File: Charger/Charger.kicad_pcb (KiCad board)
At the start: 2 copper layers, 106 parts, among them J1 Bat_ballanser_conn, J2 Battery_conn, Q1 BC846BW, Q10 MJD45H11T4, Q11 MJD45H11T4, Q12 MJD45H11T4, Q13 BC846BW, Q14 MJD31CT4, Q15 BUJ302AD, Q16 BUJ302AD, Q17 IRF7404, Q18 IRF7404, Q19 BC846BW, Q2 BC846BW, Q3 BC846BW, Q4 MJD45H11T4, Q5 MJD45H11T4, Q6 MJD45H11T4, Q7 BC846BW, Q8 BC846BW, Q9 BC846BW, U1 LM2904, U10 MCP6001-OT, U11 MCP6001-OT, U12 ACS712xLCTR-20A, U2 LM2904, U3 LM2904, U4 LM2904, U5 LM2904, U6 LM2904, U7 MCP6001-OT, U8 MCP6001-OT, U9 MCP6001-OT

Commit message: rozpoczęcie PCB
zrobiony balanser
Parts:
- added C16: 1uF, Capacitor_SMD:C_0805_2012Metric_Pad1.18x1.45mm_HandSolder, F.Cu at (-99.2, 61.8)
- added C17: 1uF, Capacitor_SMD:C_0805_2012Metric_Pad1.18x1.45mm_HandSolder, F.Cu at (-99.2, 64.8)
- added C18: 1uF, Capacitor_SMD:C_0805_2012Metric_Pad1.18x1.45mm_HandSolder, F.Cu at (-99.2, 67.8)
- added C19: 1uF, Capacitor_SMD:C_0805_2012Metric_Pad1.18x1.45mm_HandSolder, F.Cu at (-99.2, 70.8)
- added C20: 1uF, Capacitor_SMD:C_0805_2012Metric_Pad1.18x1.45mm_HandSolder, F.Cu at (-99.2, 73.8)
- added C21: 1uF, Capacitor_SMD:C_0805_2012Metric_Pad1.18x1.45mm_HandSolder, F.Cu at (-99.2, 76.8)
- added C22: 470u, Library:CP_Elec_12.5x13.5, F.Cu at (-114.6, 72.0)
- added C23: 470u, Library:CP_Elec_12.5x13.5, F.Cu at (-114.6, 86.6)
- added C24: 470u, Library:CP_Elec_12.5x13.5, F.Cu at (-20.3, 42.8)
- added C25: 470u, Library:CP_Elec_12.5x13.5, F.Cu at (-20.3, 57.4)
- added C26: 22u, Capacitor_SMD:CP_Elec_4x5.4, F.Cu at (-15.4, 67.7)
- added C27: 100n, Capacitor_SMD:C_0805_2012Metric_Pad1.18x1.45mm_HandSolder, F.Cu at (-10.0, 37.1)
- added C28: 100n, Capacitor_SMD:C_0805_2012Metric_Pad1.18x1.45mm_HandSolder, F.Cu at (-10.0, 40.1)
- added C29: 100n, Capacitor_SMD:C_0805_2012Metric_Pad1.18x1.45mm_HandSolder, F.Cu at (-10.0, 43.1)
- added C30: 22u, Capacitor_SMD:CP_Elec_4x5.4, F.Cu at (-15.4, 73.5)
- added C31: 100n, Capacitor_SMD:C_0805_2012Metric_Pad1.18x1.45mm_HandSolder, F.Cu at (-10.0, 46.1)
- added C7: 470u, Library:CP_Elec_12.5x13.5, F.Cu at (-114.6, 42.8)
- added C8: 470u, Library:CP_Elec_12.5x13.5, F.Cu at (-114.6, 57.4)
- added D1: LL103A, Diode_SMD:D_MiniMELF, F.Cu at (-82.8, 73.7)
- added D2: LL103A, Diode_SMD:D_MiniMELF, F.Cu at (-82.8, 77.1)
- added D3: LL103A, Diode_SMD:D_MiniMELF, F.Cu at (-82.8, 80.4)
- added D4: B540C, Diode_SMD:D_3220_8050Metric_Pad2.65x5.15mm_HandSolder, F.Cu at (-91.4, 75.5)
- added D5: B540C, Diode_SMD:D_3220_8050Metric_Pad2.65x5.15mm_HandSolder, F.Cu at (-91.4, 82.3)
- added D6: SS26, Diode_SMD:D_SMA, F.Cu at (-25.1, 75.3)
- added J3: Power_conn, Connector_AMASS:AMASS_XT60PW-F_1x02_P7.20mm_Horizontal, F.Cu at (-16.9, 115.9)
- added L1: 47uH, Inductor_SMD:L_Bourns_SRP1038C_10.0x10.0mm, F.Cu at (-82.0, 41.5)
- added L2: 47uH, Inductor_SMD:L_Bourns_SRP1038C_10.0x10.0mm, F.Cu at (-82.0, 53.3)
- added L3: 330u, Inductor_SMD:L_Bourns_SRR1208_12.7x12.7mm, F.Cu at (-39.1, 67.4)
- added R61: 10k, Resistor_SMD:R_0805_2012Metric_Pad1.20x1.40mm_HandSolder, F.Cu at (-94.4, 64.7)
- added R62: 5.1k, Resistor_SMD:R_0805_2012Metric_Pad1.20x1.40mm_HandSolder, F.Cu at (-94.4, 67.7)
- added R63: 1.2k, Resistor_SMD:R_0805_2012Metric_Pad1.20x1.40mm_HandSolder, F.Cu at (-94.4, 70.6)
- added R64: 10K, Resistor_SMD:R_0805_2012Metric_Pad1.20x1.40mm_HandSolder, F.Cu at (-89.7, 61.8)
- added R65: 10K, Resistor_SMD:R_0805_2012Metric_Pad1.20x1.40mm_HandSolder, F.Cu at (-89.7, 64.7)
- added R66: 10k, Resistor_SMD:R_0805_2012Metric_Pad1.20x1.40mm_HandSolder, F.Cu at (-89.7, 67.7)
- added R67: 1.2k, Resistor_SMD:R_0805_2012Metric_Pad1.20x1.40mm_HandSolder, F.Cu at (-89.7, 70.6)
- added R68: 10k, Resistor_SMD:R_0805_2012Metric_Pad1.20x1.40mm_HandSolder, F.Cu at (-84.9, 61.8)
- added R69: 1.2k, Resistor_SMD:R_0805_2012Metric_Pad1.20x1.40mm_HandSolder, F.Cu at (-84.9, 64.7)
- added R70: 2k, Resistor_SMD:R_0805_2012Metric_Pad1.20x1.40mm_HandSolder, F.Cu at (-84.9, 67.7)
- added R71: 1.2k, Resistor_SMD:R_0805_2012Metric_Pad1.20x1.40mm_HandSolder, F.Cu at (-84.9, 70.6)
- added U13: MCP6001-OT, Package_TO_SOT_SMD:SOT-23-5, F.Cu at (-104.2, 62.7)
- added U14: MCP6001-OT, Package_TO_SOT_SMD:SOT-23-5, F.Cu at (-104.2, 67.3)
- added U15: MCP6001-OT, Package_TO_SOT_SMD:SOT-23-5, F.Cu at (-104.2, 71.9)
- added U16: MCP6001-OT, Package_TO_SOT_SMD:SOT-23-5, F.Cu at (-104.2, 76.5)
- added U17: XL4015, Package_TO_SOT_SMD:TO-263-5_TabPin3, F.Cu at (-96.0, 41.8)
- added U18: XL4015, Package_TO_SOT_SMD:TO-263-5_TabPin3, F.Cu at (-96.0, 54.1)
- added U19: MCP6001-OT, Package_TO_SOT_SMD:SOT-23-5, F.Cu at (-104.2, 81.2)
- added U20: LM2575-12BU, Package_TO_SOT_SMD:TO-263-5_TabPin3, F.Cu at (-36.1, 41.8)
- added U21: L7805, Package_TO_SOT_SMD:TO-263-2, F.Cu at (-36.1, 54.1)
- added U22: LDI1117-3.3, Package_TO_SOT_SMD:SOT-223-3_TabPin2, F.Cu at (-24.2, 69.0)
- added U23: RaspberryPi_Pico, Module_RaspberryPi_Pico:RaspberryPi_Pico_Common, F.Cu at (-60.9, 83.7)
- R13, R14, R15, R16, R17, R18, R19, R20, R21, R28, R29, R30, R34, R35, R36, R37, R38, R39, R40, R41, R42, R7, R8, R9: moved to B.Cu
- R44: value 5.1k -> 2k
- moved U12 297.4 mm to (-68.8, 129.3), turned to 0 degrees
- moved Q17 288.9 mm to (-68.8, 116.2)
- moved R55 286.4 mm to (-62.2, 120.2), turned to 0 degrees
- moved C9 285.4 mm to (-57.4, 114.3)
- moved R46 284.1 mm to (-62.2, 117.2), turned to 0 degrees
- moved Q18 282.6 mm to (-68.8, 122.7), turned to 0 degrees
- moved C10 282.5 mm to (-57.4, 117.3)
- moved R56 282.5 mm to (-62.2, 123.1), turned to 0 degrees
- moved R45 282.3 mm to (-62.2, 114.3), turned to 0 degrees
- moved U10 281.3 mm to (-62.0, 127.0), turned to 0 degrees
- moved Q19 276.3 mm to (-57.2, 126.6), turned to 0 degrees
- moved C11 275.8 mm to (-57.4, 120.3)
- moved J2 270.1 mm to (-41.7, 97.0), turned to 0 degrees
- moved R44 189.1 mm to (-94.4, 61.8)
- moved R50 143.5 mm to (-27.2, 131.3)
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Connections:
- net /Pomiar pradu/P+ renamed /Ladowarka/Vout
- net /Pomiar pradu/hall_sensor renamed /Ladowarka/Hall
- R44 pad 1: Net-(R44-Pad1) -> GND
- R44 pad 2: Net-(U7-+) -> Net-(R44-Pad2)
- R47 pad 2: Net-(R44-Pad1) -> Net-(U7-+)
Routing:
- net GND: track 46.3 -> 0.00 mm
- net /Balanser/Vballans: track 62.8 -> 106.5 mm
- net +12V: track 57.9 -> 14.5 mm
- net /Balanser/B5: track 62.5 -> 26.6 mm, vias 36 -> 41
- net /Balanser/B4: track 53.3 -> 22.8 mm, vias 36 -> 41
- net /Balanser/B6: track 54.7 -> 30.1 mm
- net /Balanser/B3: track 45.9 -> 22.3 mm, vias 36 -> 41
- net /Balanser/B2: track 44.4 -> 26.2 mm, vias 36 -> 41
- net /Balanser/B1: track 51.7 -> 36.3 mm, vias 72 -> 41
- net Net-(U1A--): track 9.68 -> 21.9 mm, vias 0 -> 2
- net Net-(U5A--): track 8.18 -> 19.1 mm, vias 0 -> 2
- net Net-(U4A--): track 8.26 -> 19.1 mm, vias 0 -> 2
- net Net-(U2A--): track 8.92 -> 19.7 mm, vias 0 -> 2
- net Net-(U3A--): track 8.31 -> 18.9 mm, vias 0 -> 2
- net Net-(R13-Pad1): track 0.00 -> 3.97 mm, vias 0 -> 1
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- added copper zone on B.Cu, net (none)
- added copper zone on F.Cu, net (none)

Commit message: pcb up
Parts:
- removed C14: 100n, Capacitor_SMD:C_0805_2012Metric_Pad1.18x1.45mm_HandSolder
- removed U11, U14, U15, U16, U7, U8, U9: MCP6001-OT, Package_TO_SOT_SMD:SOT-23-5
- added C32: 1u, Capacitor_SMD:C_0805_2012Metric_Pad1.18x1.45mm_HandSolder, F.Cu at (119.3, 86.2)
- added C33: 1u, Capacitor_SMD:C_0805_2012Metric_Pad1.18x1.45mm_HandSolder, F.Cu at (101.0, 86.4)
- added C34: 1u, Capacitor_SMD:C_0805_2012Metric_Pad1.18x1.45mm_HandSolder, F.Cu at (114.9, 86.2)
- added C35: 1u, Capacitor_SMD:C_0805_2012Metric_Pad1.18x1.45mm_HandSolder, F.Cu at (129.5, 86.4)
- added C36: 100n, Capacitor_SMD:C_0805_2012Metric_Pad1.18x1.45mm_HandSolder, F.Cu at (99.1, 56.4)
- added C37: 100n, Capacitor_SMD:C_0805_2012Metric_Pad1.18x1.45mm_HandSolder, F.Cu at (155.8, 62.3)
- added C38: 100n, Capacitor_SMD:C_0805_2012Metric_Pad1.18x1.45mm_HandSolder, F.Cu at (103.1, 125.5)
- added D7: SS26, Diode_SMD:D_SMA, F.Cu at (119.0, 126.4)
- added F1: Fuse_Small, Fuse:Fuse_2010_5025Metric_Pad1.52x2.65mm_HandSolder, F.Cu at (125.8, 126.4)
- added F2: Fuse_Small, Fuse:Fuse_2010_5025Metric_Pad1.52x2.65mm_HandSolder, F.Cu at (211.8, 109.5)
- added J4: Screen_SPInCtrlnPwr_Conn, Connector_PinHeader_2.54mm:PinHeader_1x10_P2.54mm_Vertical, F.Cu at (144.3, 54.6)
- added J5: User_Interface_Conn, Connector_PinHeader_2.54mm:PinHeader_1x07_P2.54mm_Horizontal, F.Cu at (149.4, 83.5)
- added J6: 1/0_Select_Conn, Connector_PinHeader_2.54mm:PinHeader_1x03_P2.54mm_Vertical, F.Cu at (124.0, 50.2)
- added J8: Temp_Sens_Conn, Connector_PinHeader_2.54mm:PinHeader_1x03_P2.54mm_Vertical, F.Cu at (105.6, 85.6)
- added R72: 10k, Resistor_SMD:R_0805_2012Metric_Pad1.20x1.40mm_HandSolder, F.Cu at (95.9, 83.0)
- added R73: 1.2k, Resistor_SMD:R_0805_2012Metric_Pad1.20x1.40mm_HandSolder, F.Cu at (119.3, 82.8)
- added R75: 1.2k, Resistor_SMD:R_0805_2012Metric_Pad1.20x1.40mm_HandSolder, F.Cu at (100.9, 83.0)
- added R76: 1.2k, Resistor_SMD:R_0805_2012Metric_Pad1.20x1.40mm_HandSolder, F.Cu at (114.9, 82.8)
- added R77: 1.2k, Resistor_SMD:R_0805_2012Metric_Pad1.20x1.40mm_HandSolder, F.Cu at (124.3, 82.8)
- added R78: 10k, Resistor_SMD:R_0805_2012Metric_Pad1.20x1.40mm_HandSolder, F.Cu at (124.4, 86.2)
- added R79: 10k, Resistor_SMD:R_0805_2012Metric_Pad1.20x1.40mm_HandSolder, F.Cu at (129.4, 82.8)
- added U24: CD4051B, Package_SO:SO-16_5.3x10.2mm_P1.27mm, F.Cu at (153.0, 69.4)
- added U25: MCP6004, Package_SO:SOIC-14_3.9x8.7mm_P1.27mm, F.Cu at (62.0, 160.6)
- U13: value MCP6001-OT -> MCP6004; footprint Package_TO_SOT_SMD:SOT-23-5 -> Package_SO:SOIC-14_3.9x8.7mm_P1.27mm
- U23: footprint Module_RaspberryPi_Pico:RaspberryPi_Pico_Common -> Module_RaspberryPi_Pico:RaspberryPi_Pico_Common_SMD
- moved C8 322.5 mm to (192.9, 154.7), turned to 90 degrees
- moved C22 302.1 mm to (175.8, 155.4), turned to 90 degrees
- moved C20 296.1 mm to (190.2, 136.3), turned to -90 degrees
- moved C7 293.0 mm to (155.6, 156.2)
- moved C23 291.6 mm to (164.1, 172.4), turned to -90 degrees
- moved U17 282.8 mm to (170.2, 137.3), turned to -90 degrees
- moved D4 280.8 mm to (181.7, 140.9)
- moved L1 279.9 mm to (182.9, 131.8)
- moved Q16 275.1 mm to (233.7, 112.4), turned to 90 degrees
- moved C18 273.6 mm to (168.4, 124.6), turned to -90 degrees
- moved C17 271.9 mm to (166.1, 124.6), turned to 90 degrees
- moved U18 267.4 mm to (158.1, 137.3), turned to -90 degrees
- moved Q15 267.1 mm to (226.3, 112.4), turned to 90 degrees
- moved C19 261.2 mm to (156.3, 124.7), turned to -90 degrees
- moved C16 260.9 mm to (154.0, 124.7), turned to 90 degrees
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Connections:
- C12 pad 1: /Sztuczne_obciazenie/+5V -> +5V
- C13 pad 1: /Sztuczne_obciazenie/+5V -> +5V
- C15 pad 1: /Sztuczne_obciazenie/+5V -> +5V
- C16 pad 1: /Ladowarka/Vin -> +36V
- C17 pad 1: /Ladowarka/Vin -> +36V
- C18 pad 1: /Ladowarka/Vin -> +36V
- C19 pad 1: /Ladowarka/Vin -> +36V
- C23 pad 1: /Ladowarka/Vin -> +36V
- C25 pad 1: /Ladowarka/Vin -> +36V
- C7 pad 1: /Ladowarka/Vin -> +36V
- D1 pad 2: /Ladowarka/Off -> GPIO2
- J3 pad 2: /Ladowarka/Vin -> Net-(J3-Pin_2)
- Q14 pad 2: /Ladowarka/Vout -> /Sztuczne_obciazenie/B+
- Q15 pad 2: /Ladowarka/Vout -> /Sztuczne_obciazenie/B+
- Q16 pad 2: /Ladowarka/Vout -> /Sztuczne_obciazenie/B+
- Q19 pad 1: /Pomiar pradu/P_ON -> GPIO10
- R47 pad 1: /Sztuczne_obciazenie/set_I -> /MCU/LOAD_SetI
- R47 pad 2: Net-(U7-+) -> Net-(U13A-+)
- R48 pad 2: Net-(U7-+) -> Net-(U13A-+)
- R49 pad 1: /Sztuczne_obciazenie/EN -> GPIO8
- R49 pad 2: Net-(U8-+) -> Net-(U13C-+)
- R50 pad 2: Net-(U8-+) -> Net-(U13C-+)
- R51 pad 2: Net-(U9--) -> Net-(U13B--)
- R52 pad 1: Net-(U9--) -> Net-(U13B--)
- R52 pad 2: Net-(U11-+) -> Net-(U13D-+)
- R53 pad 1: Net-(U8--) -> Net-(U13C--)
- R53 pad 2: Net-(U9-+) -> Net-(U13B-+)
- R54 pad 1: Net-(U7--) -> Net-(U13A--)
- R54 pad 2: Net-(U9-+) -> Net-(U13B-+)
- R59 pad 2: /Ladowarka/Vout -> /Sztuczne_obciazenie/B+
- R61 pad 1: Net-(U13-+) -> Net-(U25A-+)
- R62 pad 2: Net-(U13-+) -> Net-(U25A-+)
- R64 pad 2: Net-(U13--) -> Net-(U25A--)
- U13 pad 1: Net-(U13--) -> Net-(U13A--)
- U13 pad 2: GND -> Net-(U13A--)
- U13 pad 3: Net-(U13-+) -> Net-(U13A-+)
- U13 pad 4: Net-(U13--) -> +5V
- U13 pad 5: +5V -> Net-(U13B-+)
- U17 pad 5: /Ladowarka/Vin -> +36V
- U18 pad 5: /Ladowarka/Vin -> +36V
- U20 pad 1: /Ladowarka/Vin -> +36V
- U23 pad 10: unconnected-(U23-GPIO7-Pad10) -> GPIO7
- U23 pad 11: unconnected-(U23-GPIO8-Pad11) -> GPIO8
- U23 pad 12: unconnected-(U23-GPIO9-Pad12) -> GPIO9
- U23 pad 14: unconnected-(U23-GPIO10-Pad14) -> GPIO10
- U23 pad 15: unconnected-(U23-GPIO11-Pad15) -> GPIO11
- U23 pad 16: unconnected-(U23-GPIO12-Pad16) -> GPIO12
- U23 pad 17: unconnected-(U23-GPIO13-Pad17) -> GPIO13
- U23 pad 19: unconnected-(U23-GPIO14-Pad19) -> GPIO14
- U23 pad 20: unconnected-(U23-GPIO15-Pad20) -> GPIO15
- U23 pad 21: unconnected-(U23-GPIO16-Pad21) -> GPIO16
- U23 pad 22: unconnected-(U23-GPIO17-Pad22) -> GPIO17
- U23 pad 24: unconnected-(U23-GPIO18-Pad24) -> GPIO18
- U23 pad 25: unconnected-(U23-GPIO19-Pad25) -> GPIO19
- U23 pad 26: unconnected-(U23-GPIO20-Pad26) -> GPIO20
- U23 pad 27: unconnected-(U23-GPIO21-Pad27) -> GPIO21
- U23 pad 29: unconnected-(U23-GPIO22-Pad29) -> GPIO22
- U23 pad 31: unconnected-(U23-GPIO26_ADC0-Pad31) -> ADC_0
- U23 pad 32: unconnected-(U23-GPIO27_ADC1-Pad32) -> GPIO27
- U23 pad 33: unconnected-(U23-AGND-Pad33) -> GND
- U23 pad 34: unconnected-(U23-GPIO28_ADC2-Pad34) -> GPIO28
- U23 pad 39: unconnected-(U23-VSYS-Pad39) -> +5V
- U23 pad 4: unconnected-(U23-GPIO2-Pad4) -> GPIO2
- U23 pad 5: unconnected-(U23-GPIO3-Pad5) -> GPIO3
- U23 pad 6: unconnected-(U23-GPIO4-Pad6) -> GPIO4
- U23 pad 9: unconnected-(U23-GPIO6-Pad9) -> GPIO6

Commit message: small update
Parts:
- F1: value Fuse_Small -> 10A
- moved C25 43.6 mm to (147.9, 173.8)
- moved C24 14.3 mm to (123.7, 165.5)
- moved J6 5.05 mm to (129.1, 50.2), turned to -90 degrees
- moved C22 1.78 mm to (177.4, 154.6)
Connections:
- J4 pad 2: GPIO19 -> GPIO16
- J4 pad 3: GPIO16 -> GPIO17
- J4 pad 4: GPIO17 -> GPIO18
- J4 pad 5: GPIO18 -> GPIO19
- J5 pad 2: GPIO14 -> GPIO15
- J5 pad 3: GPIO15 -> GPIO14

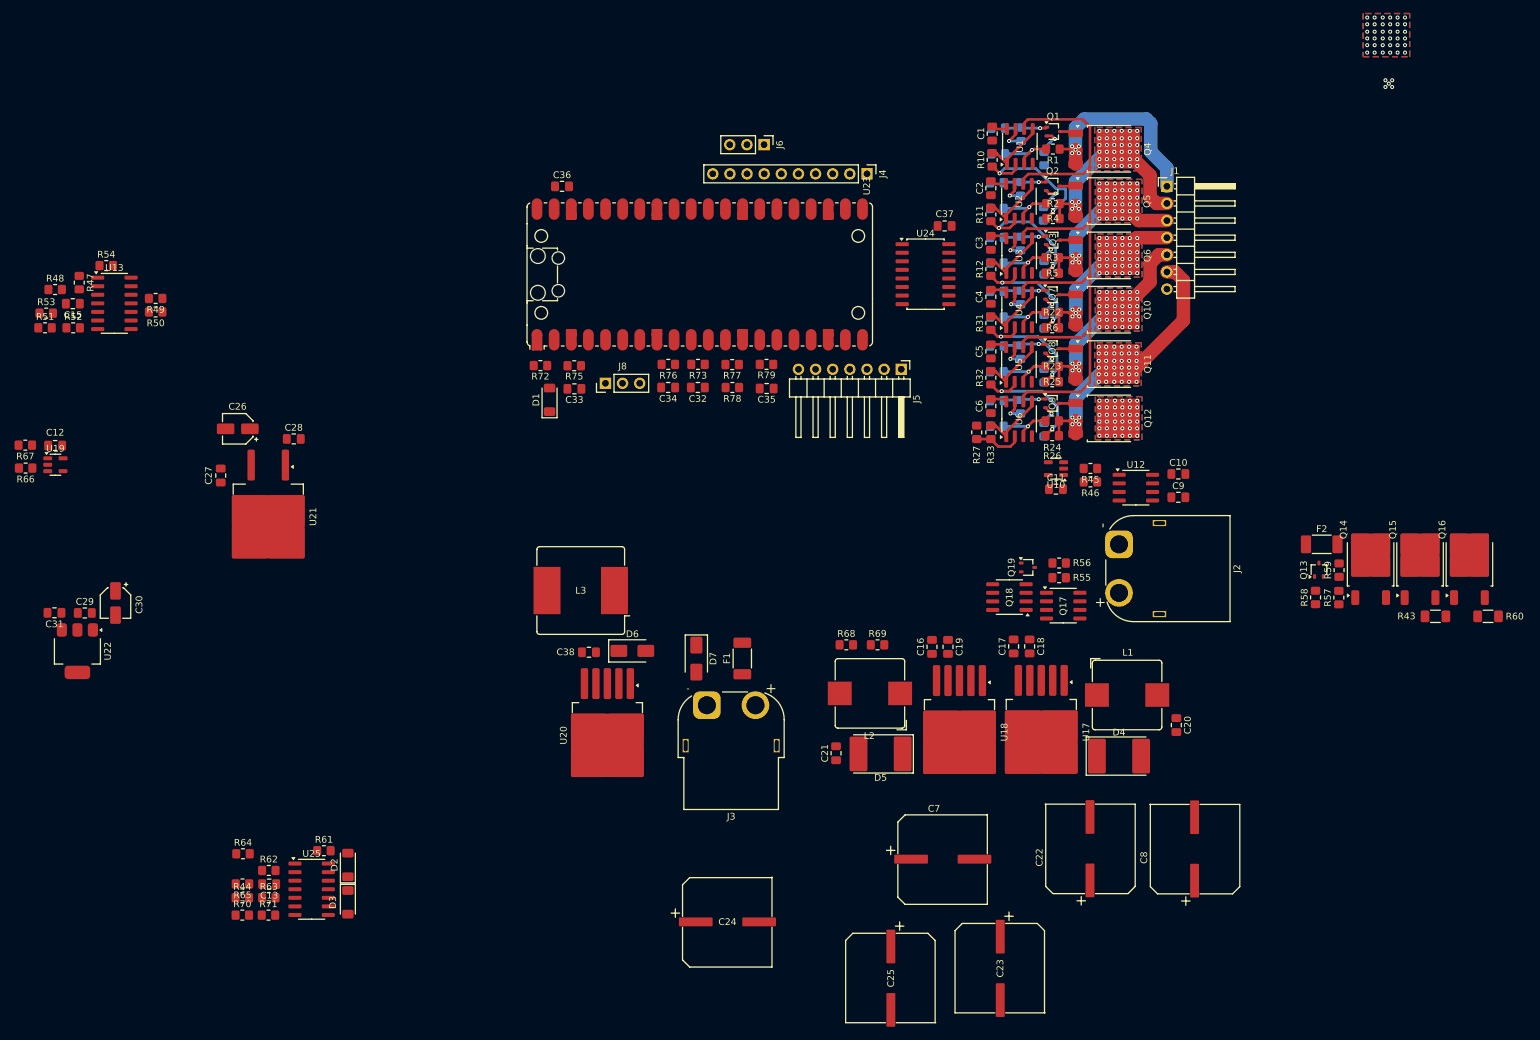
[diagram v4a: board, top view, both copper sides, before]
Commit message: pcb poukladane
usuniete 3 kondensatory
brak poligonow i odprowadzania ciepla
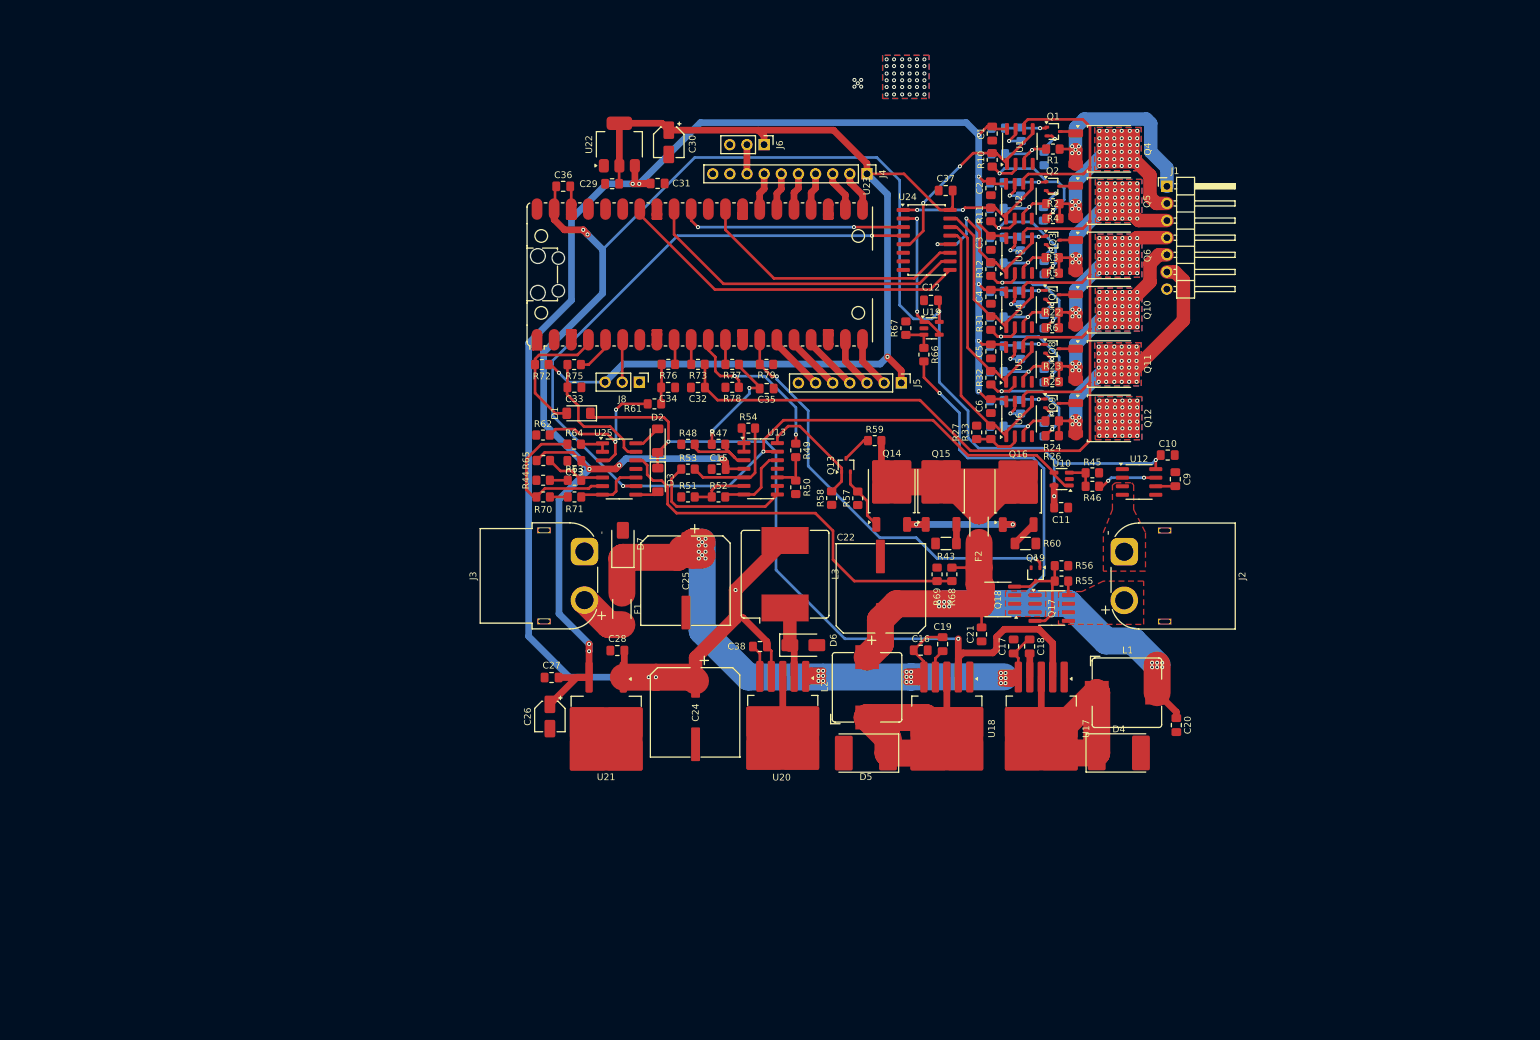
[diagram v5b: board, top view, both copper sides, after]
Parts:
- removed C23, C7, C8: 470u, Library:CP_Elec_12.5x13.5
- J5: footprint Connector_PinHeader_2.54mm:PinHeader_1x07_P2.54mm_Horizontal -> Connector_PinHeader_2.54mm:PinHeader_1x07_P2.54mm_Vertical
- moved R66 134.2 mm to (152.8, 81.4), turned to -90 degrees
- moved R67 131.7 mm to (150.1, 77.5), turned to -90 degrees
- moved C12 131.6 mm to (153.8, 73.3)
- moved U19 131.5 mm to (153.9, 77.5)
- moved U22 110.0 mm to (107.6, 50.2), turned to 90 degrees
- moved C31 109.8 mm to (113.3, 56.0), turned to 0 degrees
- moved C30 106.7 mm to (115.0, 49.9)
- moved C29 100.8 mm to (106.5, 56.0), turned to 180 degrees
- moved U13 98.9 mm to (128.6, 98.3)
- moved R52 98.9 mm to (122.3, 102.5)
- moved C15 98.8 mm to (122.3, 98.3)
- moved R51 98.6 mm to (117.8, 102.5)
- moved R50 98.4 mm to (133.8, 101.0), turned to 90 degrees
- moved R54 98.2 mm to (126.8, 92.3)
- moved R53 97.9 mm to (117.8, 98.3)
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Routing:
- net +5V: track 0.00 -> 279.0 mm, vias 0 -> 10
- net +12V: track 14.5 -> 279.8 mm, vias 0 -> 11
- net /Ladowarka/Hall: track 0.00 -> 163.9 mm, vias 0 -> 3
- net +3.3V: track 0.00 -> 155.7 mm, vias 0 -> 2
- net /Ladowarka/Vout: track 0.00 -> 142.4 mm, vias 0 -> 13
- net +36V: track 0.00 -> 123.9 mm, vias 0 -> 28
- net FB: track 0.00 -> 116.2 mm, vias 0 -> 2
- net /Balanser/Vballans: track 106.5 -> 180.2 mm
- net GPIO10: track 0.00 -> 64.0 mm, vias 0 -> 2
- net Ref: track 0.00 -> 59.1 mm
- net GPIO28: track 0.00 -> 51.8 mm
- net GPIO27: track 0.00 -> 48.3 mm
- net GPIO22: track 0.00 -> 40.6 mm
- net Net-(D5-K): track 0.00 -> 38.4 mm
- net Net-(D4-K): track 0.00 -> 38.2 mm
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- added copper zone on F.Cu, net /Pomiar pradu/BAT+
- added copper zone on F.Cu, net /Pomiar pradu/BAT-
- added copper zone on F.Cu, net Net-(Q17-S-Pad1)
